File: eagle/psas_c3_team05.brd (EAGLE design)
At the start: 100 x 71.1 mm, 84 parts, among them IC1 CP2102, Q1 32 MHz, U1 MIC5219 3.3V, U2 MCP73871

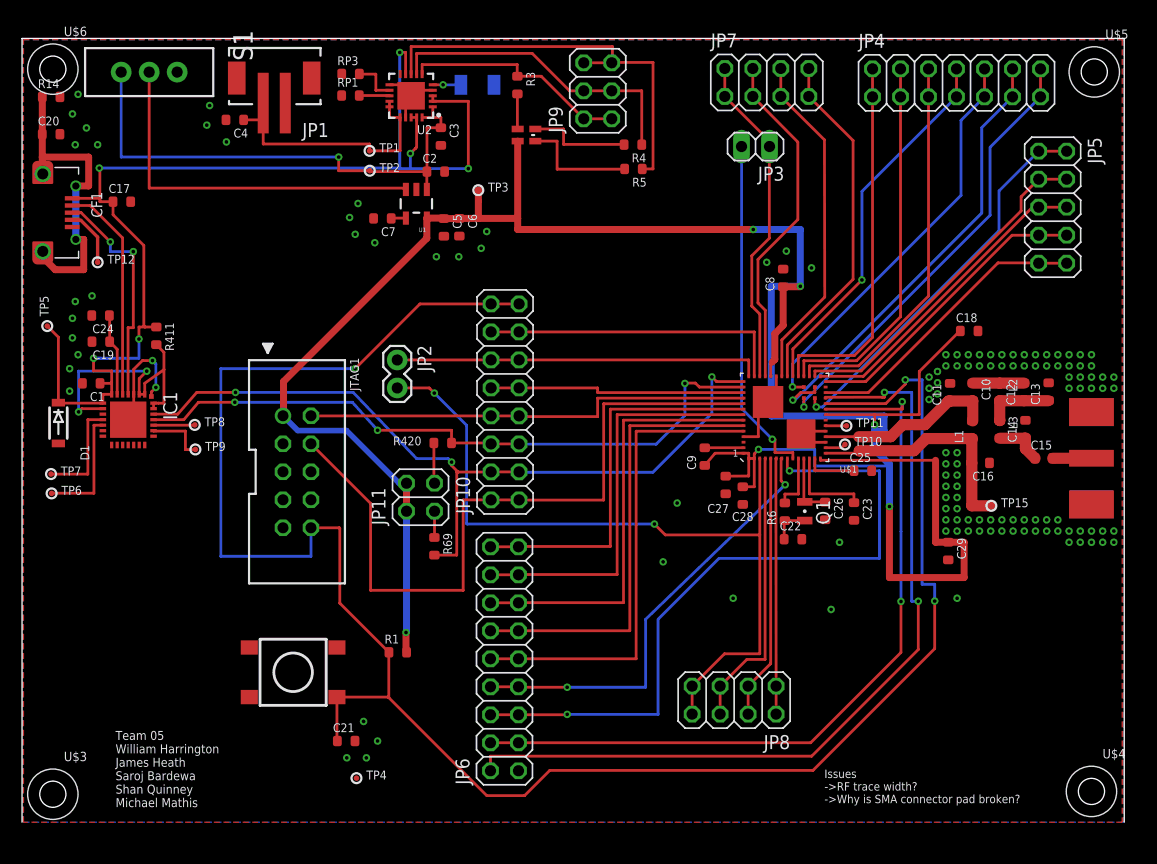
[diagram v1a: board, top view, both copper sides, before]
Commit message: Layout reconfig and got rid of sch component
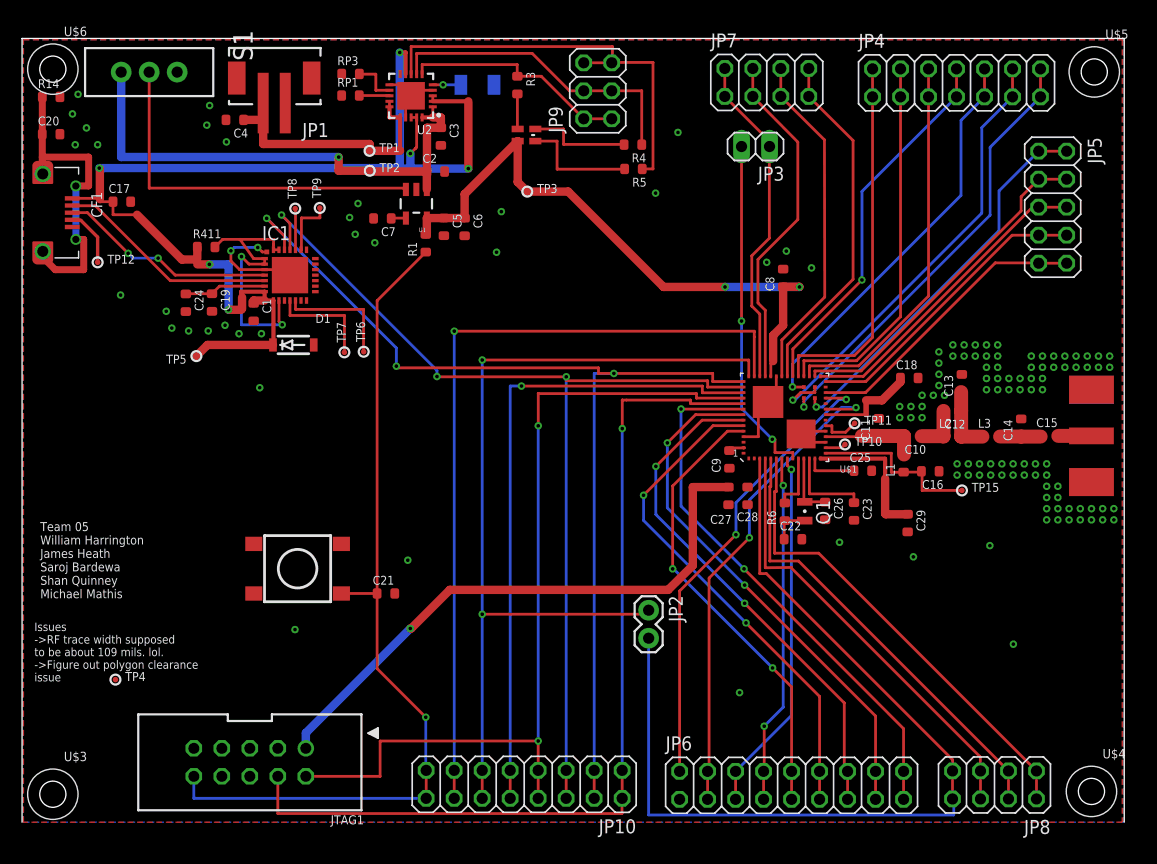
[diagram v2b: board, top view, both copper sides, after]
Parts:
- removed JP11: (no value), pinhead:2X02
- removed R420, R69: 4.7k, rcl_custom:.0603-B-NOSILK
- moved R1 37.2 mm to (36.6, 52.5), turned to 90 degrees
- moved JP10 34.7 mm to (45.6, 3.44), turned to 180 degrees
- moved JP2 32.2 mm to (56.9, 19.2)
- moved TP6 31.1 mm to (31.0, 42.7), turned to 90 degrees
- moved TP7 28.8 mm to (29.2, 42.6), turned to 90 degrees
- moved JP6 28.5 mm to (69.8, 3.35), turned to 0 degrees
- moved JTAG1 26.7 mm to (20.7, 5.43), turned to 180 degrees
- moved JP8 24.8 mm to (88.2, 3.38)
- moved TP9 24.6 mm to (27.0, 55.7), turned to 90 degrees
- moved TP4 23.6 mm to (8.47, 12.9)
- moved D1 22.5 mm to (24.6, 43.3), turned to 0 degrees
- moved TP8 21.6 mm to (24.8, 55.7), turned to 90 degrees
- moved IC1 19.7 mm to (24.3, 49.6), turned to 0 degrees
- moved C1 16.1 mm to (21.0, 46.3), turned to 270 degrees
- moved C21 13.9 mm to (33.0, 20.8)
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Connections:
- removed net N$28: JP11.1, R69.1
- removed net N$29: JP11.3, R420.1
- net 3.3V: no longer JP11.2, JP11.4
- net PTA1: no longer R69.2
- net PTA2: no longer R420.2
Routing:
- net PTA20/!RESET: track 180.0 -> 79.6 mm, vias 3 -> 1
- net 3.3V: track 230.2 -> 132.5 mm, vias 6 -> 3
- net PTA18: track 33.4 -> 80.9 mm, vias 0 -> 2
- net N$27: track 27.9 -> 73.7 mm, vias 0 -> 1
- net PTA3: track 40.9 -> 80.1 mm, vias 0 -> 2
- net N$26: track 23.3 -> 59.2 mm, vias 0 -> 1
- net PTE0: track 76.4 -> 42.4 mm
- net PTE2: track 63.7 -> 33.2 mm, vias 2 -> 1
- net PTA2: track 60.7 -> 91.0 mm
- net PTE1: track 71.1 -> 44.7 mm
- net PTA1: track 73.1 -> 95.0 mm
- net N$16: track 23.2 -> 43.2 mm
- net N$20: track 24.1 -> 41.5 mm
- net PTA0: track 66.4 -> 83.5 mm, vias 0 -> 1
- net N$23: track 25.9 -> 40.4 mm
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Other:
- board text added: "Issues ->RF trace width supposed to be about 109 mils. lol. ->Figure out polygon clearance issue"
- board text removed: "Issues ->RF trace width? ->Why is SMA connector pad broken?"

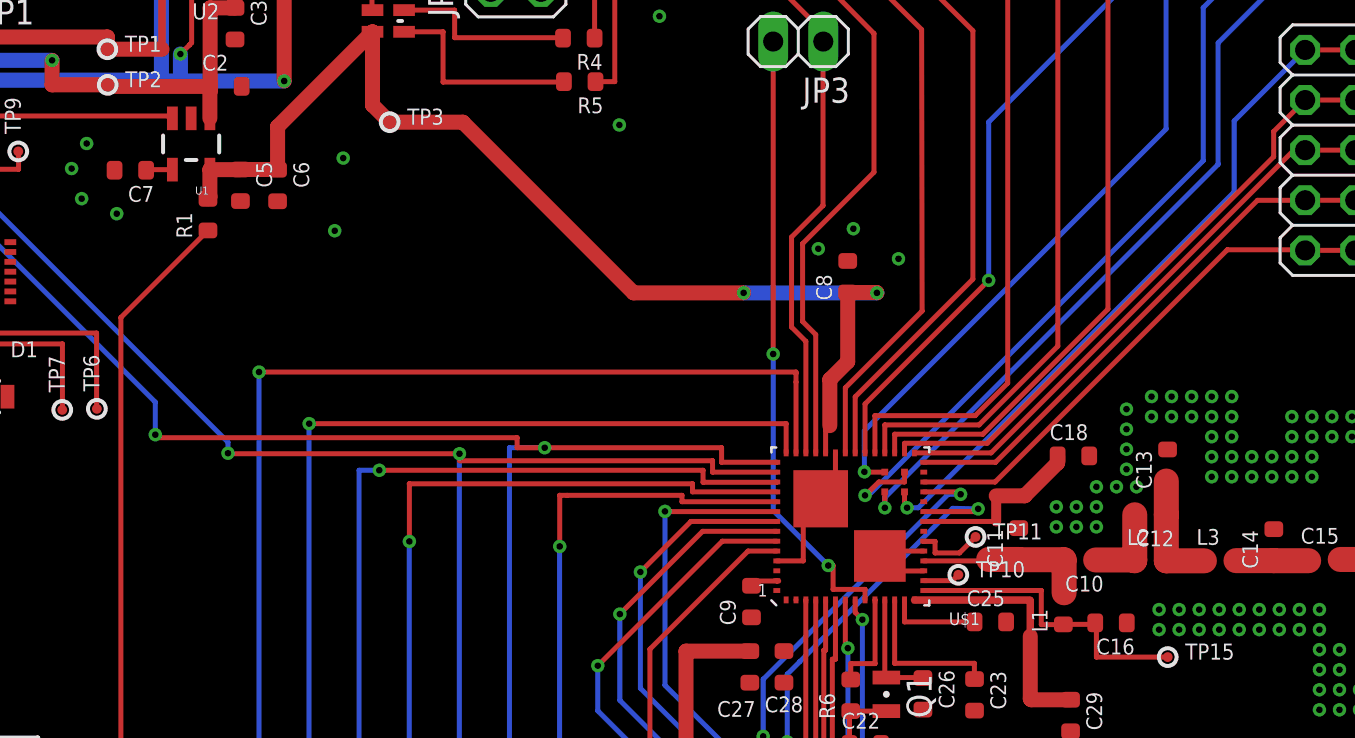
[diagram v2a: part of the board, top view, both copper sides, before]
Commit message: put in reset line
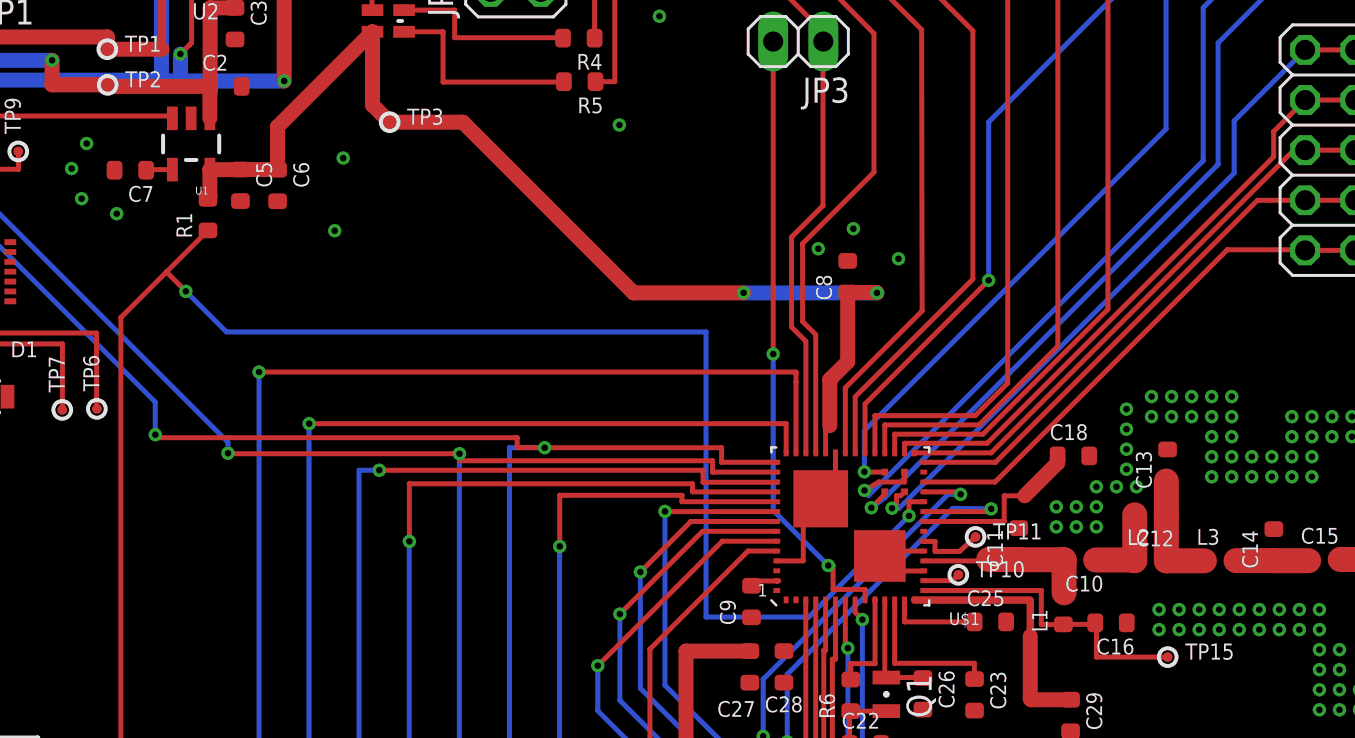
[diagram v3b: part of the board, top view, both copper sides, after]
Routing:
- net PTA20/!RESET: track 79.6 -> 136.6 mm, vias 1 -> 3
- net PTE1: track 44.7 -> 46.1 mm
- net PTC7: track 40.4 -> 41.0 mm
- net PTD0: track 35.3 -> 35.9 mm
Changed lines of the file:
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@@
 <wire x1="78.359" y1="27.94" x2="80.350359375" y2="27.94" width="0.762" layer="1"/>
 <wire x1="80.350359375" y1="27.94" x2="80.350359375" y2="27.9424375" width="0.254" layer="1"/>
-<wire x1="72.909521875" y1="36.9784" x2="76.581" y2="36.9784" width="0.254" layer="1"/>
-<wire x1="76.581" y1="36.9784" x2="76.581" y2="38.2778" width="0.508" layer="1"/>
-<wire x1="76.581" y1="38.2778" x2="78.02635625" y2="38.2778" width="0.762" layer="1"/>
+<wire x1="72.909521875" y1="36.9784" x2="76.9874" y2="36.9784" width="0.254" layer="1"/>
+<wire x1="76.9874" y1="36.9784" x2="76.9874" y2="38.2778" width="0.254" layer="1"/>
+<wire x1="76.9874" y1="38.2778" x2="78.02635625" y2="38.2778" width="0.254" layer="1"/>
 <wire x1="36.725903125" y1="54.811034375" x2="38.268109375" y2="54.811034375" width="0.762" layer="1"/>
 <wire x1="38.268109375" y1="54.811034375" x2="38.275259375" y2="54.818184375" width="0.254" layer="1"/>
@@
 <wire x1="32.214921875" y1="13.936878125" x2="36.6268" y2="9.525" width="0.254" layer="1"/>
 <wire x1="32.214921875" y1="20.7543375" x2="32.214921875" y2="47.315321875" width="0.254" layer="1"/>
-<wire x1="32.214921875" y1="47.315321875" x2="36.629340625" y2="51.729740625" width="0.254" layer="1"/>
+<wire x1="32.214921875" y1="47.315321875" x2="34.5249" y2="49.6253" width="0.254" layer="1"/>
+<wire x1="34.5249" y1="49.6253" x2="36.629340625" y2="51.729740625" width="0.254" layer="1"/>
 <wire x1="28.976221875" y1="20.752240625" x2="32.212825" y2="20.752240625" width="0.254" layer="1"/>
 <wire x1="32.212825" y1="20.752240625" x2="32.214921875" y2="20.7543375" width="0.254" layer="1"/>
-<wire x1="36.629340625" y1="51.729740625" x2="72.909521875" y2="37.9784" width="0" layer="19" extent="1-1"/>
+<wire x1="72.1106" y1="37.338" x2="72.1614" y2="37.2618" width="0.254" layer="1"/>
+<via x="72.1614" y="37.2618" extent="1-16" drill="0.3302"/>
+<wire x1="72.1614" y1="37.2618" x2="67.0814" y2="32.131" width="0.254" layer="16"/>
+<wire x1="67.0814" y1="32.131" x2="61.8744" y2="32.131" width="0.254" layer="16"/>
+<wire x1="61.8744" y1="32.131" x2="61.8744" y2="46.5836" width="0.254" layer="16"/>
+<wire x1="61.8744" y1="46.5836" x2="37.5666" y2="46.5836" width="0.254" layer="16"/>
+<wire x1="37.5666" y1="46.5836" x2="35.5092" y2="48.641" width="0.254" layer="16"/>
+<via x="35.5092" y="48.641" extent="1-16" drill="0.3302"/>
+<wire x1="35.5092" y1="48.641" x2="34.5249" y2="49.6253" width="0.254" layer="1"/>
+<wire x1="72.909521875" y1="37.9784" x2="72.1614" y2="37.9784" width="0.254" layer="1"/>
+<wire x1="72.1614" y1="37.9784" x2="72.1614" y2="37.2618" width="0.254" layer="1"/>
 </signal>
 <signal name="XTA">
@@
 <wire x1="72.909521875" y1="35.9664" x2="72.909521875" y2="35.9784" width="0.254" layer="1"/>
 <wire x1="72.909521875" y1="35.9664" x2="73.4822" y2="35.9664" width="0.254" layer="1"/>
-<wire x1="73.4822" y1="35.9664" x2="73.4822" y2="35.3822" width="0.254" layer="1"/>
-<wire x1="73.4822" y1="35.3822" x2="74.721721875" y2="35.3822" width="0.254" layer="1"/>
-<wire x1="74.721721875" y1="35.3822" x2="75.534521875" y2="36.195" width="0.254" layer="1"/>
+<wire x1="73.4822" y1="35.9664" x2="73.4822" y2="35.4584" width="0.254" layer="1"/>
+<wire x1="73.4822" y1="35.4584" x2="74.721721875" y2="35.4584" width="0.254" layer="1"/>
+<wire x1="74.721721875" y1="35.4584" x2="75.534521875" y2="36.195" width="0.254" layer="1"/>
 </signal>
 <signal name="RESET(RF)">
@@
 <wire x1="71.934521875" y1="39.4784" x2="71.934521875" y2="38.978840625" width="0.254" layer="1"/>
 <wire x1="71.934521875" y1="38.978840625" x2="70.637403125" y2="38.978840625" width="0.254" layer="1"/>
-<wire x1="70.637403125" y1="38.978840625" x2="69.93128125" y2="38.29811875" width="0.254" layer="1"/>
-<via x="69.93128125" y="38.29811875" extent="1-16" drill="0.3302"/>
-<wire x1="69.93128125" y1="38.29811875" x2="70.109078125" y2="38.29811875" width="0.254" layer="16"/>
+<wire x1="70.637403125" y1="38.978840625" x2="69.90588125" y2="38.55211875" width="0.254" layer="1"/>
+<via x="69.90588125" y="38.55211875" extent="1-16" drill="0.3302"/>
+<wire x1="69.90588125" y1="38.55211875" x2="70.109078125" y2="38.29811875" width="0.254" layer="16"/>
 <wire x1="70.109078125" y1="38.29811875" x2="87.073740625" y2="55.26278125" width="0.254" layer="16"/>
 <wire x1="87.073740625" y1="55.26278125" x2="87.073740625" y2="63.019940625" width="0.254" layer="16"/>
@@
 <contactref element="JP4" pad="13"/>
 <wire x1="92.4052" y1="68.3514" x2="92.4052" y2="65.8114" width="0.254" layer="1"/>
-<wire x1="70.934521875" y1="38.4784" x2="70.934521875" y2="37.6733375" width="0.254" layer="1"/>
-<wire x1="70.934521875" y1="37.6733375" x2="70.93711875" y2="37.670740625" width="0.254" layer="1"/>
-<via x="70.93711875" y="37.670740625" extent="1-16" drill="0.3302"/>
-<wire x1="70.93711875" y1="37.670740625" x2="70.93711875" y2="38.186359375" width="0.254" layer="16"/>
+<via x="70.25131875" y="37.670740625" extent="1-16" drill="0.3302"/>
+<wire x1="70.25131875" y1="37.670740625" x2="70.93711875" y2="38.186359375" width="0.254" layer="16"/>
 <wire x1="70.93711875" y1="38.186359375" x2="87.830659375" y2="55.0799" width="0.254" layer="16"/>
 <wire x1="87.830659375" y1="55.0799" x2="87.830659375" y2="61.236859375" width="0.254" layer="16"/>
 <wire x1="87.830659375" y1="61.236859375" x2="92.4052" y2="65.8114" width="0.254" layer="16"/>
+<wire x1="70.934521875" y1="38.4784" x2="70.934521875" y2="38.35394375" width="0.254" layer="1"/>
+<wire x1="70.934521875" y1="38.35394375" x2="70.25131875" y2="37.670740625" width="0.254" layer="1"/>
 </signal>
 <signal name="PTD0">
@@
 <contactref element="JP5" pad="1"/>
 <wire x1="94.7801" y1="60.878721875" x2="92.2401" y2="60.878721875" width="0.254" layer="1"/>
-<wire x1="71.934521875" y1="38.4784" x2="71.934521875" y2="37.78585625" width="0.254" layer="1"/>
-<wire x1="71.934521875" y1="37.78585625" x2="72.0623375" y2="37.673278125" width="0.254" layer="1"/>
-<via x="72.0623375" y="37.673278125" extent="1-16" drill="0.3302"/>
-<wire x1="72.0623375" y1="37.673278125" x2="72.631296875" y2="37.673278125" width="0.254" layer="16"/>
-<wire x1="72.631296875" y1="37.673278125" x2="88.643459375" y2="53.685440625" width="0.254" layer="16"/>
-<wire x1="88.643459375" y1="53.685440625" x2="88.643459375" y2="57.28208125" width="0.254" layer="16"/>
+<via x="71.3003375" y="37.647878125" extent="1-16" drill="0.3302"/>
 <wire x1="88.643459375" y1="57.28208125" x2="92.2401" y2="60.878721875" width="0.254" layer="16"/>
+<wire x1="71.3003375" y1="37.647878125" x2="71.658478125" y2="37.647878125" width="0.254" layer="16"/>
+<wire x1="71.658478125" y1="37.647878125" x2="88.643459375" y2="54.632859375" width="0.254" layer="16"/>
+<wire x1="88.643459375" y1="54.632859375" x2="88.643459375" y2="57.28208125" width="0.254" layer="16"/>
+<wire x1="71.5306625" y1="38.2820625" x2="71.5264" y2="38.2778" width="0.254" layer="1"/>
+<wire x1="71.5264" y1="38.2778" x2="71.5264" y2="37.873940625" width="0.254" layer="1"/>
+<wire x1="71.5264" y1="37.873940625" x2="71.3003375" y2="37.647878125" width="0.254" layer="1"/>
+<wire x1="71.5306625" y1="38.2820625" x2="71.738184375" y2="38.2820625" width="0.254" layer="1"/>
+<wire x1="71.738184375" y1="38.2820625" x2="71.934521875" y2="38.4784" width="0.254" layer="1"/>
 </signal>
 <signal name="PTD4">
@@
 <via x="65.9892" y="25.8064" extent="1-16" drill="0.3302"/>
 <wire x1="65.9892" y1="25.8064" x2="65.9892" y2="29.2354" width="0.254" layer="16"/>
-<via x="75.6666" y="37.6174" extent="1-16" drill="0.3302"/>
+<via x="76.327" y="37.6174" extent="1-16" drill="0.3302"/>
 <wire x1="65.9892" y1="29.2354" x2="66.6242" y2="29.8704" width="0.254" layer="16"/>
 <wire x1="66.6242" y1="29.8704" x2="74.3712" y2="37.6428" width="0.254" layer="16"/>
-<wire x1="74.3712" y1="37.6428" x2="75.6666" y2="37.6174" width="0.254" layer="16"/>
-<wire x1="72.909521875" y1="37.4784" x2="75.5784" y2="37.4784" width="0.254" layer="1"/>
-<wire x1="75.5784" y1="37.4784" x2="75.6666" y2="37.6174" width="0.254" layer="1"/>
+<wire x1="74.3712" y1="37.6428" x2="76.327" y2="37.6174" width="0.254" layer="16"/>
+<wire x1="72.909521875" y1="37.4784" x2="76.327" y2="37.4784" width="0.254" layer="1"/>
+<wire x1="76.327" y1="37.4784" x2="76.327" y2="37.6174" width="0.254" layer="1"/>
 </signal>
 <signal name="PTE2">
